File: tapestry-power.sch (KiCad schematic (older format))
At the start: 15 parts, among them J1 4.5-20V, J2 4.5-20V, J3 5V, U1 sic450

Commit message: basic board
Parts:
- L1: footprint Inductor_SMD:L_12x12mm_H6mm -> libs:IP67GZ01
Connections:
- net VHIGH: now reaches L1.1, U1.26 (SW), U1.27 (SW), U1.28 (SW), U1.29 (SW), U1.30 (SW), U1.31 (SW)
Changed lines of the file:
@@
 F 0 "L1" H 3800 1965 50  0000 C CNN
 F 1 "INDUCTOR" H 3800 1874 50  0000 C CNN
-F 2 "Inductor_SMD:L_12x12mm_H6mm" H 3800 1750 50  0001 C CNN
+F 2 "libs:IP67GZ01" H 3800 1750 50  0001 C CNN
 F 3 "~" H 3800 1750 50  0001 C CNN
 	1    3800 1750
@@
 Wire Wire Line
 	9900 2050 9800 2050
+Text Label 3300 1750 0    50   ~ 0
+VHIGH
 $EndSCHEMATC

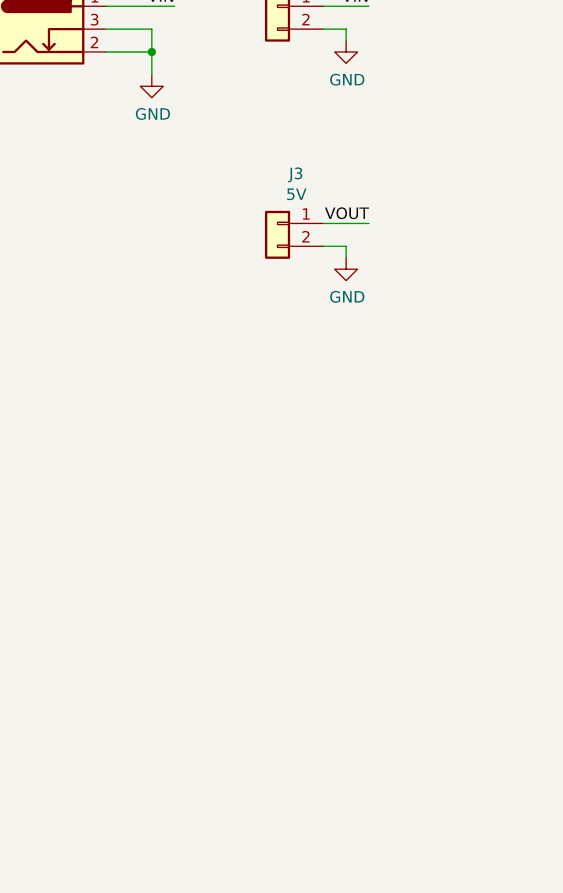
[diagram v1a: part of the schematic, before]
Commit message: Tightened up pours.  Added Fiducials
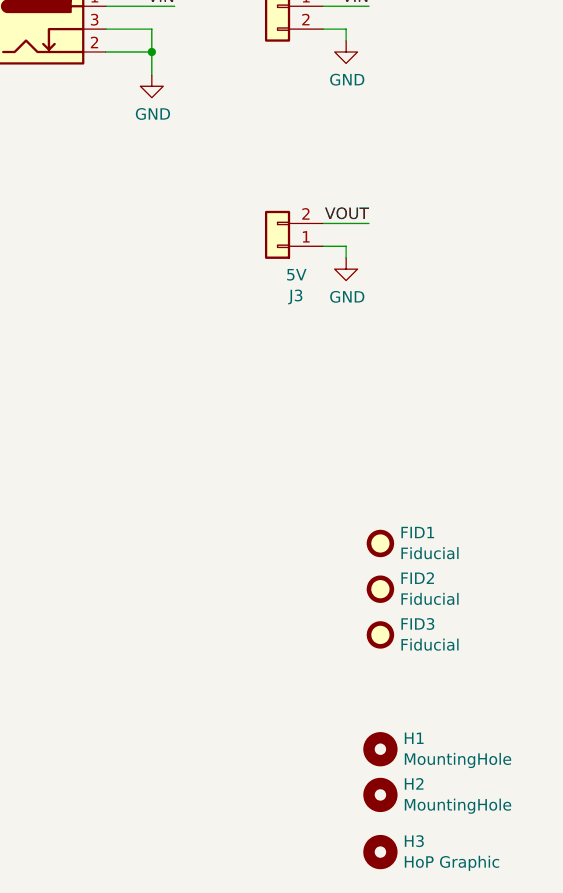
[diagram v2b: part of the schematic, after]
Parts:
- added FID1, FID2, FID3: Fiducial, Fiducial:Fiducial_0.5mm_Mask1mm, symbol Mechanical:Fiducial
- added H1, H2: MountingHole, MountingHole:MountingHole_3.2mm_M3, symbol Mechanical:MountingHole
- added H3: HoP Graphic, libs:HoP_logo, symbol Mechanical:MountingHole
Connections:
- net GND: now also J3.1 (Pin_1); no longer J3.2 (Pin_2)
- net VOUT: now also J3.2 (Pin_2); no longer J3.1 (Pin_1)
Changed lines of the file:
@@
 L Connector_Generic:Conn_01x02 J3
 U 1 1 60BAB04D
-P 9600 1950
-F 0 "J3" H 9518 2167 50  0000 C CNN
-F 1 "5V" H 9518 2076 50  0000 C CNN
-F 2 "libs:p2034a-dinkle-2-way-5mm" H 9600 1950 50  0001 C CNN
-F 3 "~" H 9600 1950 50  0001 C CNN
-	1    9600 1950
-	-1   0    0    -1
+P 9600 2050
+F 0 "J3" H 9518 2267 50  0000 C CNN
+F 1 "5V" H 9518 2176 50  0000 C CNN
+F 2 "libs:p2034a-dinkle-2-way-5mm" H 9600 2050 50  0001 C CNN
+F 3 "~" H 9600 2050 50  0001 C CNN
+	1    9600 2050
+	-1   0    0    1
 $EndComp
 $Comp
@@
 Text Label 3300 1750 0    50   ~ 0
 VHIGH
+$Comp
+L Mechanical:Fiducial FID1
+U 1 1 60E03B62
+P 10050 3350
+F 0 "FID1" H 10135 3396 50  0000 L CNN
+F 1 "Fiducial" H 10135 3305 50  0000 L CNN
+F 2 "Fiducial:Fiducial_0.5mm_Mask1mm" H 10050 3350 50  0001 C CNN
+F 3 "~" H 10050 3350 50  0001 C CNN
+	1    10050 3350
+	1    0    0    -1
+$EndComp
+$Comp
+L Mechanical:Fiducial FID2
+U 1 1 60E048E3
+P 10050 3550
+F 0 "FID2" H 10135 3596 50  0000 L CNN
+F 1 "Fiducial" H 10135 3505 50  0000 L CNN
+F 2 "Fiducial:Fiducial_0.5mm_Mask1mm" H 10050 3550 50  0001 C CNN
+F 3 "~" H 10050 3550 50  0001 C CNN
+	1    10050 3550
+	1    0    0    -1
+$EndComp
+$Comp
+L Mechanical:Fiducial FID3
+U 1 1 60E04EC7
+P 10050 3750
+F 0 "FID3" H 10135 3796 50  0000 L CNN
+F 1 "Fiducial" H 10135 3705 50  0000 L CNN
+F 2 "Fiducial:Fiducial_0.5mm_Mask1mm" H 10050 3750 50  0001 C CNN
+F 3 "~" H 10050 3750 50  0001 C CNN
+	1    10050 3750
+	1    0    0    -1
+$EndComp
+$Comp
+L Mechanical:MountingHole H1
+U 1 1 60E05B16
+P 10050 4250
+F 0 "H1" H 10150 4296 50  0000 L CNN
+F 1 "MountingHole" H 10150 4205 50  0000 L CNN
+F 2 "MountingHole:MountingHole_3.2mm_M3" H 10050 4250 50  0001 C CNN
+F 3 "~" H 10050 4250 50  0001 C CNN
+	1    10050 4250
+	1    0    0    -1
+$EndComp
+$Comp
+L Mechanical:MountingHole H2
+U 1 1 60E06302
+P 10050 4450
+F 0 "H2" H 10150 4496 50  0000 L CNN
+F 1 "MountingHole" H 10150 4405 50  0000 L CNN
+F 2 "MountingHole:MountingHole_3.2mm_M3" H 10050 4450 50  0001 C CNN
+F 3 "~" H 10050 4450 50  0001 C CNN
+	1    10050 4450
+	1    0    0    -1
+$EndComp
+$Comp
+L Mechanical:MountingHole H3
+U 1 1 60E15611
+P 10050 4700
+F 0 "H3" H 10150 4746 50  0000 L CNN
+F 1 "HoP Graphic" H 10150 4655 50  0000 L CNN
+F 2 "libs:HoP_logo" H 10050 4700 50  0001 C CNN
+F 3 "~" H 10050 4700 50  0001 C CNN
+	1    10050 4700
+	1    0    0    -1
+$EndComp
 $EndSCHEMATC

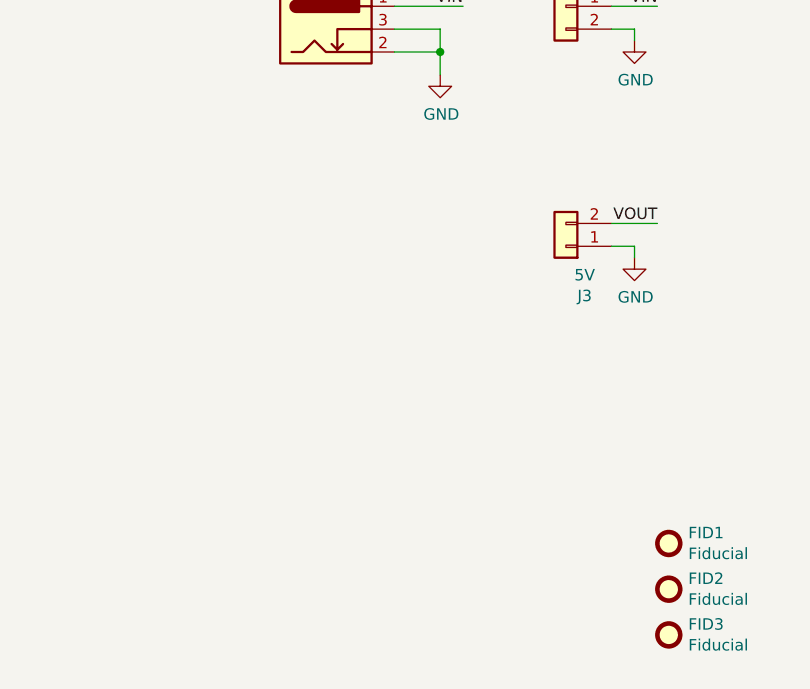
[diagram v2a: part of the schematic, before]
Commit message: Added dual footprints for solder nuts.
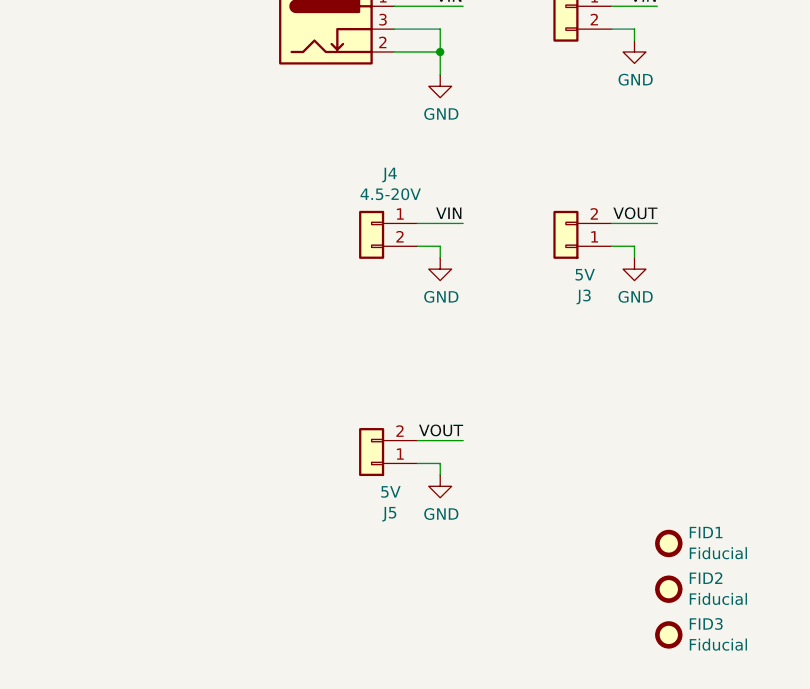
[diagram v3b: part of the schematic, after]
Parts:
- added J4: 4.5-20V, libs:Solder-Nut.2x1, symbol Connector_Generic:Conn_01x02
- added J5: 5V, libs:Solder-Nut.2x1, symbol Connector_Generic:Conn_01x02
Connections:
- net GND: now also J4.2 (Pin_2), J5.1 (Pin_1)
- net VIN: now also J4.1 (Pin_1)
- net VOUT: now also J5.2 (Pin_2)
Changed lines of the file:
@@
 	1    0    0    -1
 $EndComp
+$Comp
+L Connector_Generic:Conn_01x02 J4
+U 1 1 60F6CDFC
+P 8750 1950
+F 0 "J4" H 8668 2167 50  0000 C CNN
+F 1 "4.5-20V" H 8668 2076 50  0000 C CNN
+F 2 "libs:Solder-Nut.2x1" H 8750 1950 50  0001 C CNN
+F 3 "~" H 8750 1950 50  0001 C CNN
+	1    8750 1950
+	-1   0    0    -1
+$EndComp
+Text Label 9150 2900 2    50   ~ 0
+VOUT
+Text Label 9150 1950 2    50   ~ 0
+VIN
+$Comp
+L power:GND #PWR0109
+U 1 1 60F6D024
+P 9050 2100
+F 0 "#PWR0109" H 9050 1850 50  0001 C CNN
+F 1 "GND" H 9055 1927 50  0000 C CNN
+F 2 "" H 9050 2100 50  0001 C CNN
+F 3 "" H 9050 2100 50  0001 C CNN
+	1    9050 2100
+	1    0    0    -1
+$EndComp
+Wire Wire Line
+	8950 1950 9150 1950
+Wire Wire Line
+	9050 2100 9050 2050
+Wire Wire Line
+	9050 2050 8950 2050
+$Comp
+L Connector_Generic:Conn_01x02 J5
+U 1 1 60F6D031
+P 8750 3000
+F 0 "J5" H 8668 3217 50  0000 C CNN
+F 1 "5V" H 8668 3126 50  0000 C CNN
+F 2 "libs:Solder-Nut.2x1" H 8750 3000 50  0001 C CNN
+F 3 "~" H 8750 3000 50  0001 C CNN
+	1    8750 3000
+	-1   0    0    1
+$EndComp
+$Comp
+L power:GND #PWR0110
+U 1 1 60F6D03B
+P 9050 3050
+F 0 "#PWR0110" H 9050 2800 50  0001 C CNN
+F 1 "GND" H 9055 2877 50  0000 C CNN
+F 2 "" H 9050 3050 50  0001 C CNN
+F 3 "" H 9050 3050 50  0001 C CNN
+	1    9050 3050
+	1    0    0    -1
+$EndComp
+Wire Wire Line
+	8950 2900 9150 2900
+Wire Wire Line
+	9050 3050 9050 3000
+Wire Wire Line
+	9050 3000 8950 3000
 $EndSCHEMATC
